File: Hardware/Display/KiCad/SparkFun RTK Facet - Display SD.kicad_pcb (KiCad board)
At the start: 2 copper layers, 49.5 x 22 mm, 39 parts, among them J1 Conn_01x12_FPC_0.5mm, J2 microSD, J3 I2C, J4 Conn_01x06_FPC_1.0mm, SW1 SMD_5.2x5.2mm_h2.5mm, U1 SSD1306

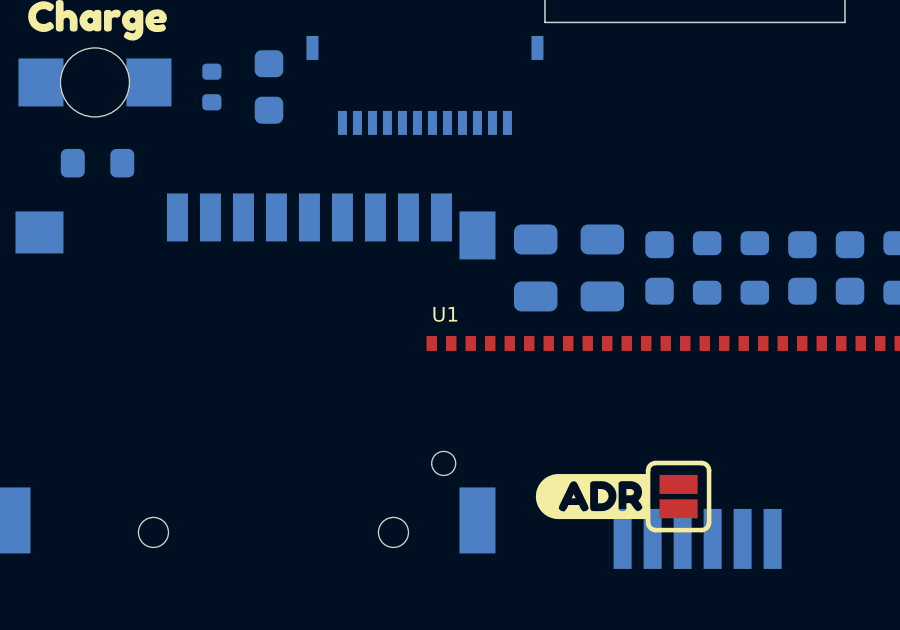
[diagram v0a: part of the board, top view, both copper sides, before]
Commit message: Fix part number on LIF
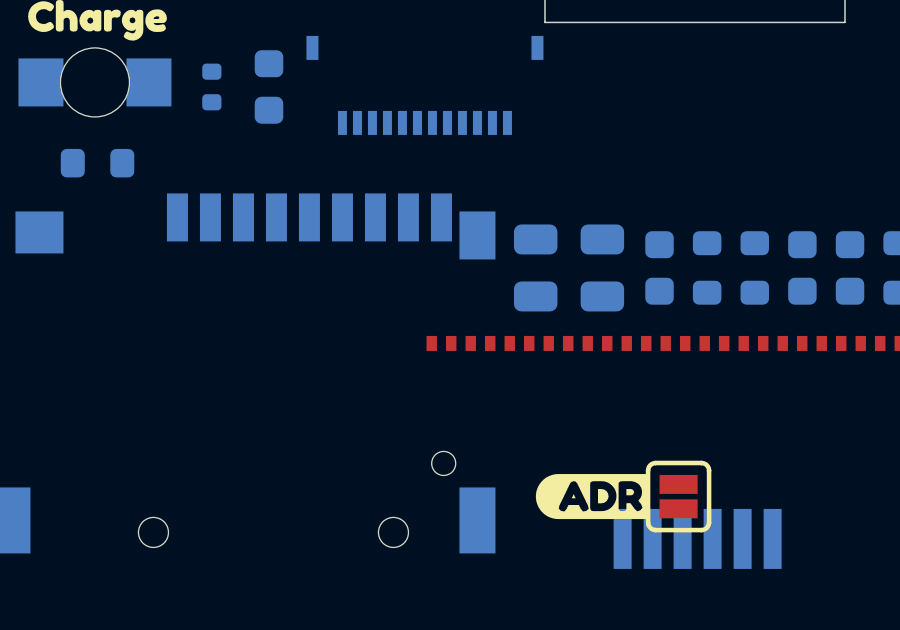
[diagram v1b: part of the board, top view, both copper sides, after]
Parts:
- D1: footprint SparkFun-LED:LED_1206-Bottom -> SparkFun-LED:LED_1206_Bottom_Green
- U1: value SSD1306 -> OLED_0.66"; footprint SparkFun RTK Facet - Display SD:OLED-0.66-64X48-TRIM -> SparkFun-Display:OLED_0.66-SMD
